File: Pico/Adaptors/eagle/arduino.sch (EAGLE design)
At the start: 6 parts, among them J1 JST-2P-SMD-PW-3410050P1

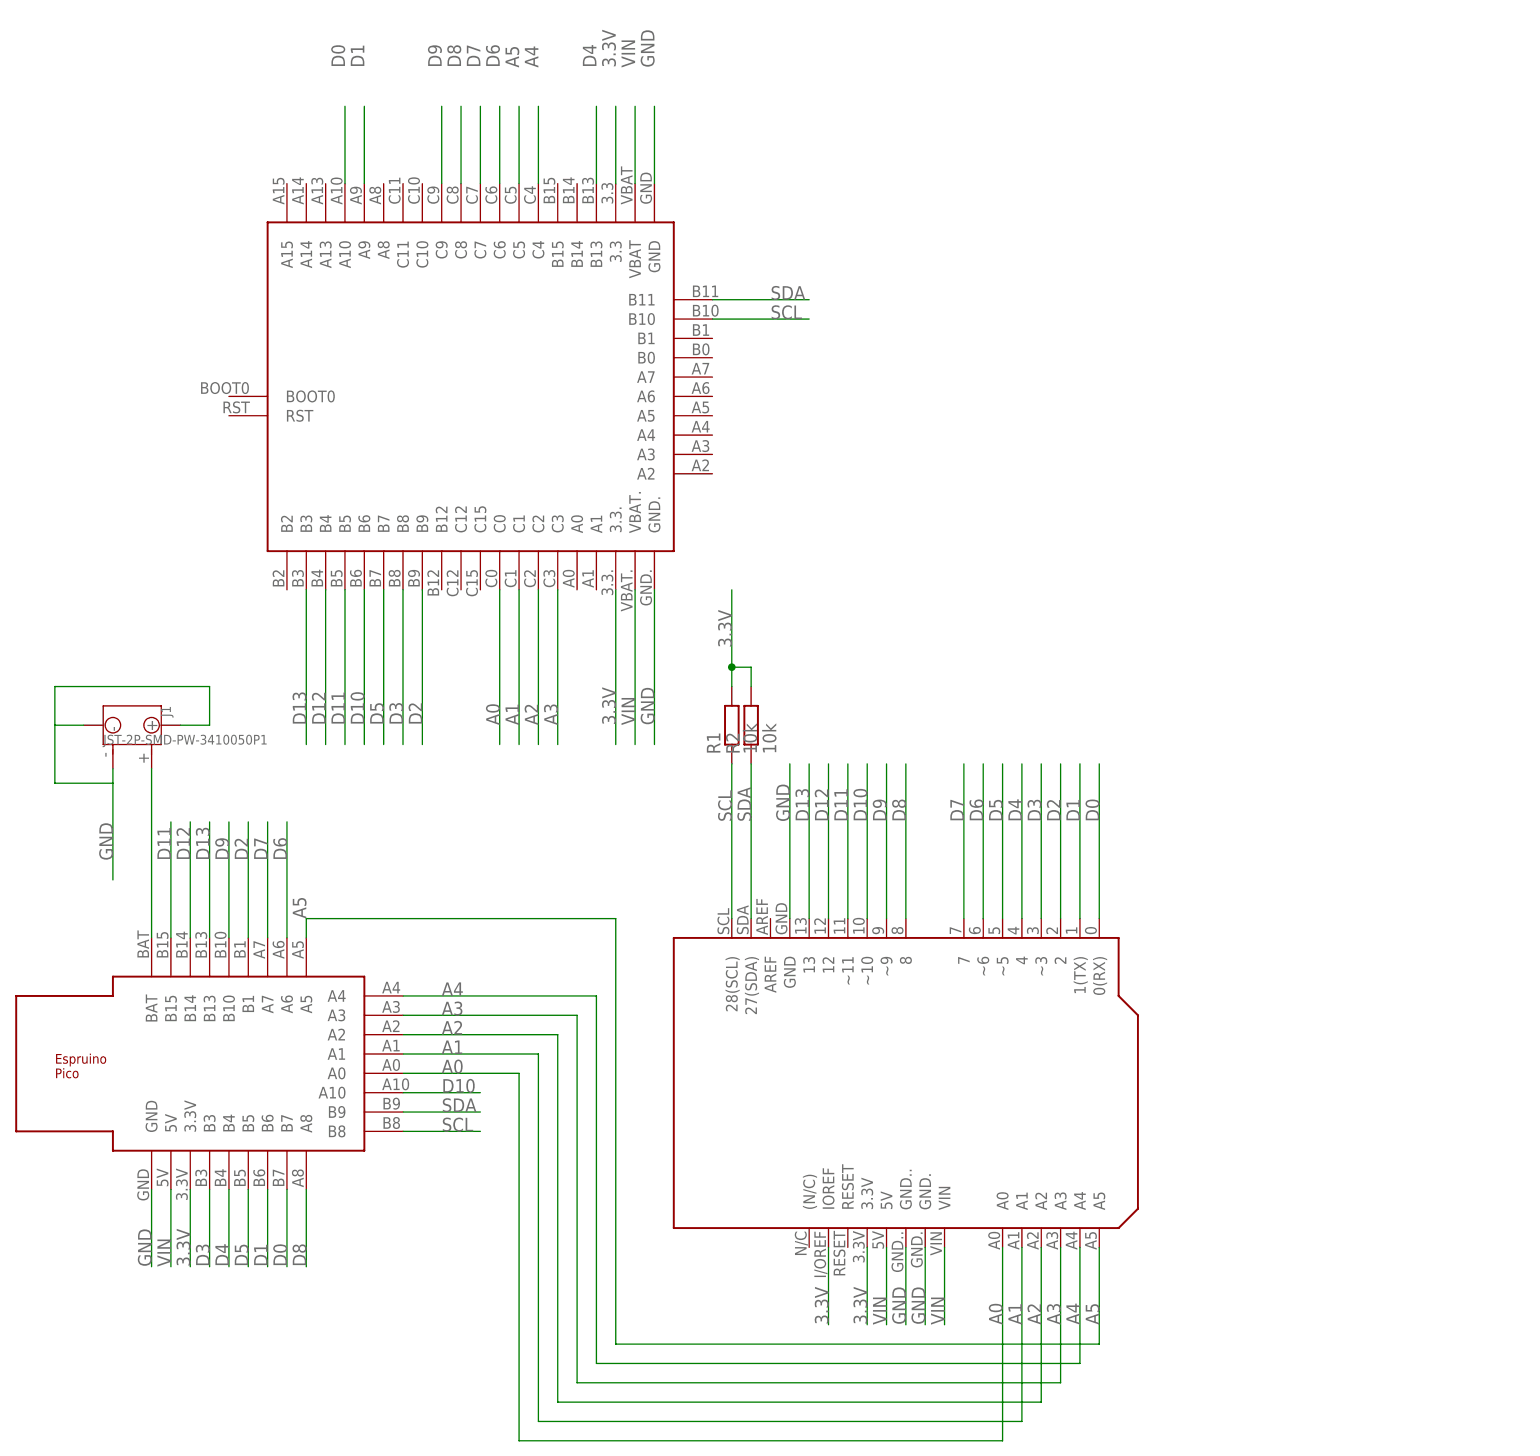
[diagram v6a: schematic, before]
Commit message: added battery charger IC
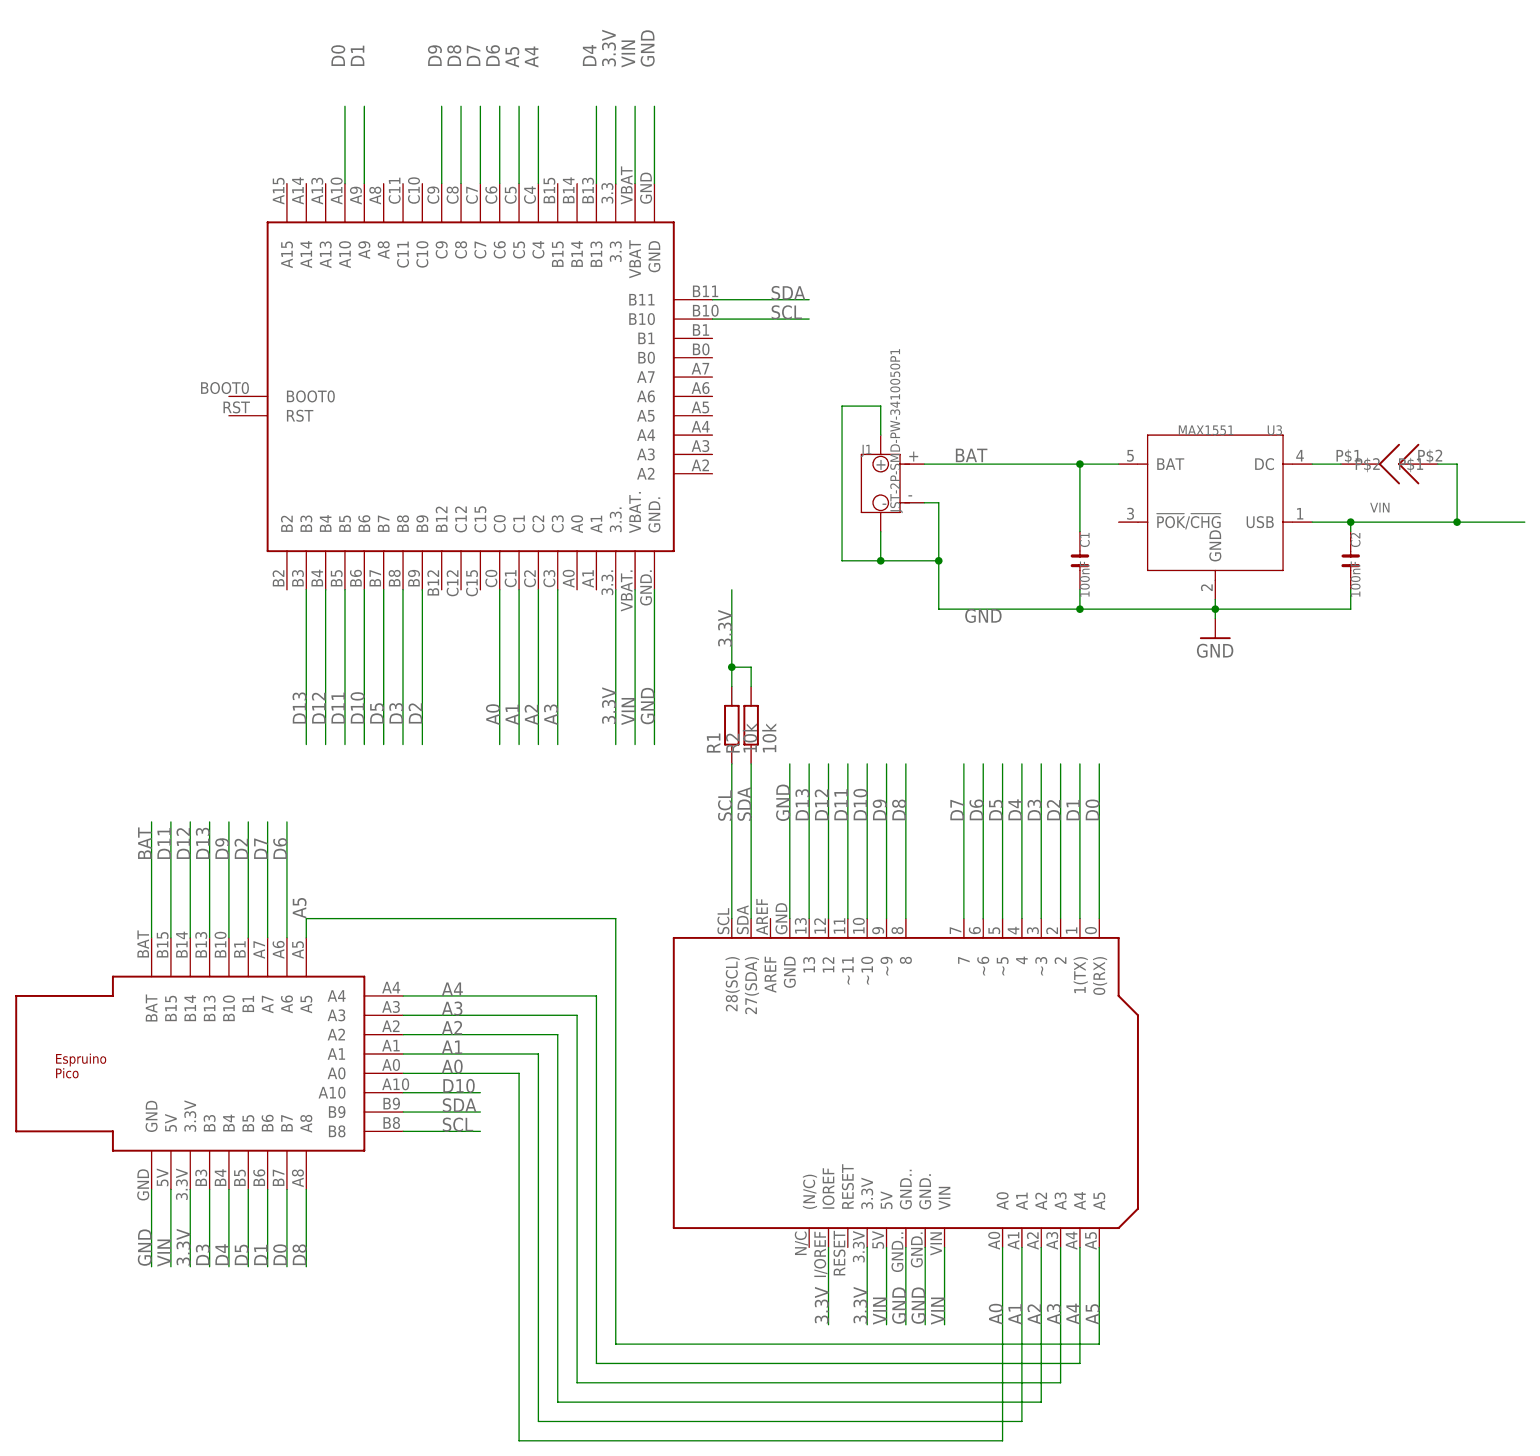
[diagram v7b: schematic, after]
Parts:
- added C1, C2: 100nF, OPL5:C-0603
- added U$4: SOLDERJUMPER, solder_jumper:SOLDERJUMPER
- added U3: MAX1551, template:MAX1551
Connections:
- removed net N$1: J1.+, U$1.BAT
- new net BAT: C1.1, J1.+, U$1.BAT, U3.BAT
- new net N$2: U$4.P$1, U3.DC
- net GND: now also C1.2, C2.2, U3.GND
- net VIN: now also C2.1, U$4.P$2, U3.USB
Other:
- moved on the sheet: J1
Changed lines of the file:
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@@
 <layer number="111" name="111" color="7" fill="1" visible="no" active="no"/>
 <layer number="112" name="tSilk" color="7" fill="1" visible="no" active="no"/>
+<layer number="113" name="IDFDebug" color="7" fill="1" visible="yes" active="yes"/>
 <layer number="116" name="Patch_BOT" color="9" fill="4" visible="yes" active="yes"/>
 <layer number="118" name="Rect_Pads" color="7" fill="1" visible="no" active="no"/>
@@
 <layer number="223" name="223bmp" color="24" fill="1" visible="no" active="no"/>
 <layer number="224" name="224bmp" color="25" fill="1" visible="no" active="no"/>
+<layer number="225" name="225bmp" color="7" fill="1" visible="yes" active="yes"/>
+<layer number="226" name="226bmp" color="7" fill="1" visible="yes" active="yes"/>
+<layer number="227" name="227bmp" color="7" fill="1" visible="yes" active="yes"/>
+<layer number="228" name="228bmp" color="7" fill="1" visible="yes" active="yes"/>
+<layer number="230" name="230bmp" color="7" fill="1" visible="no" active="yes"/>
 <layer number="248" name="Housing" color="7" fill="1" visible="no" active="no"/>
 <layer number="249" name="Edge" color="7" fill="1" visible="no" active="no"/>
@@
 <part name="R2" library="rcl" deviceset="R-EU_" device="R0805" value="10k"/>
 <part name="J1" library="OPL Eagle Library" deviceset="JST-2P-SMD-PW" device="-3410050P1"/>
+<part name="U3" library="template" deviceset="MAX1551" device="" value="MAX1551"/>
+<part name="GND26" library="supply1" deviceset="GND" device=""/>
+<part name="C2" library="OPL5" deviceset="C*" device="-0603" value="100nF"/>
+<part name="C1" library="OPL5" deviceset="C*" device="-0603" value="100nF"/>
+<part name="U$4" library="solder_jumper" deviceset="SOLDERJUMPER" device=""/>
 </parts>
 <sheets>
@@
 <instance part="R1" gate="G$1" x="60.96" y="78.74" rot="R90"/>
 <instance part="R2" gate="G$1" x="63.5" y="78.74" rot="R90"/>
-<instance part="J1" gate="J" x="-17.78" y="78.74" rot="R270"/>
+<instance part="J1" gate="J" x="80.518" y="110.49"/>
+<instance part="U3" gate="G$1" x="124.46" y="107.95" rot="MR0"/>
+<instance part="GND26" gate="1" x="124.46" y="90.17"/>
+<instance part="C2" gate="C" x="142.24" y="100.33" rot="R270"/>
+<instance part="C1" gate="C" x="106.68" y="100.33" rot="R270"/>
+<instance part="U$4" gate="G$1" x="148.59" y="113.03"/>
 </instances>
 <busses>
@@
 </segment>
 <segment>
+<pinref part="U3" gate="G$1" pin="GND"/>
+<pinref part="GND26" gate="1" pin="GND"/>
+<wire x1="124.46" y1="92.71" x2="124.46" y2="93.98" width="0.1524" layer="91"/>
+<pinref part="C1" gate="C" pin="2"/>
+<wire x1="124.46" y1="93.98" x2="124.46" y2="95.25" width="0.1524" layer="91"/>
+<wire x1="106.68" y1="96.52" x2="106.68" y2="93.98" width="0.1524" layer="91"/>
+<wire x1="106.68" y1="93.98" x2="124.46" y2="93.98" width="0.1524" layer="91"/>
+<junction x="124.46" y="93.98"/>
+<pinref part="C2" gate="C" pin="2"/>
+<wire x1="124.46" y1="93.98" x2="142.24" y2="93.98" width="0.1524" layer="91"/>
+<wire x1="142.24" y1="93.98" x2="142.24" y2="96.52" width="0.1524" layer="91"/>
 <pinref part="J1" gate="J" pin="-"/>
-<wire x1="-20.32" y1="73.025" x2="-20.32" y2="71.12" width="0.1524" layer="91"/>
-<wire x1="-20.32" y1="71.12" x2="-20.32" y2="58.42" width="0.1524" layer="91"/>
-<wire x1="-20.32" y1="71.12" x2="-27.94" y2="71.12" width="0.1524" layer="91"/>
-<wire x1="-27.94" y1="71.12" x2="-27.94" y2="78.74" width="0.1524" layer="91"/>
-<wire x1="-27.94" y1="78.74" x2="-27.94" y2="83.82" width="0.1524" layer="91"/>
-<wire x1="-27.94" y1="83.82" x2="-7.62" y2="83.82" width="0.1524" layer="91"/>
-<wire x1="-7.62" y1="83.82" x2="-7.62" y2="78.74" width="0.1524" layer="91"/>
-<wire x1="-7.62" y1="78.74" x2="-11.43" y2="78.74" width="0.1524" layer="91"/>
-<wire x1="-27.94" y1="78.74" x2="-24.13" y2="78.74" width="0.1524" layer="91"/>
+<wire x1="86.233" y1="107.95" x2="88.138" y2="107.95" width="0.1524" layer="91"/>
+<wire x1="88.138" y1="100.33" x2="88.138" y2="93.98" width="0.1524" layer="91"/>
+<wire x1="88.138" y1="107.95" x2="88.138" y2="100.33" width="0.1524" layer="91"/>
+<wire x1="88.138" y1="100.33" x2="80.518" y2="100.33" width="0.1524" layer="91"/>
+<wire x1="80.518" y1="100.33" x2="75.438" y2="100.33" width="0.1524" layer="91"/>
+<wire x1="75.438" y1="100.33" x2="75.438" y2="120.65" width="0.1524" layer="91"/>
+<wire x1="75.438" y1="120.65" x2="80.518" y2="120.65" width="0.1524" layer="91"/>
+<wire x1="80.518" y1="120.65" x2="80.518" y2="116.84" width="0.1524" layer="91"/>
+<wire x1="80.518" y1="100.33" x2="80.518" y2="104.14" width="0.1524" layer="91"/>
 <pinref part="J1" gate="J" pin="3"/>
 <pinref part="J1" gate="J" pin="4"/>
-<label x="-20.32" y="60.96" size="1.778" layer="95" rot="R90"/>
+<label x="96.52" y="93.98" size="1.778" layer="95" rot="R180"/>
+<wire x1="106.68" y1="93.98" x2="88.138" y2="93.98" width="0.1524" layer="91"/>
+<junction x="80.518" y="100.33"/>
+<junction x="88.138" y="100.33"/>
+<junction x="106.68" y="93.98"/>
 </segment>
 </net>
@@
 <wire x1="81.28" y1="10.16" x2="81.28" y2="0" width="0.1524" layer="91"/>
 <label x="81.28" y="0" size="1.778" layer="95" rot="R90"/>
+</segment>
+<segment>
+<pinref part="U3" gate="G$1" pin="USB"/>
+<wire x1="137.16" y1="105.41" x2="142.24" y2="105.41" width="0.1524" layer="91"/>
+<label x="144.78" y="106.68" size="1.27" layer="95" ratio="10"/>
+<pinref part="C2" gate="C" pin="1"/>
+<wire x1="142.24" y1="104.14" x2="142.24" y2="105.41" width="0.1524" layer="91"/>
+<junction x="142.24" y="105.41"/>
+<wire x1="142.24" y1="105.41" x2="156.21" y2="105.41" width="0.1524" layer="91"/>
+<pinref part="U$4" gate="G$1" pin="P$2"/>
+<wire x1="156.21" y1="105.41" x2="165.1" y2="105.41" width="0.1524" layer="91"/>
+<wire x1="153.67" y1="113.03" x2="156.21" y2="113.03" width="0.1524" layer="91"/>
+<wire x1="156.21" y1="113.03" x2="156.21" y2="105.41" width="0.1524" layer="91"/>
+<junction x="156.21" y="105.41"/>
+<wire x1="156.21" y1="105.41" x2="156.21" y2="105.156" width="0.1524" layer="91"/>
 </segment>
 </net>
@@
 </segment>
 </net>
-<net name="N$1" class="0">
+<net name="BAT" class="0">
 <segment>
 <pinref part="U$1" gate="G$1" pin="BAT"/>
+<wire x1="-15.24" y1="50.8" x2="-15.24" y2="66.04" width="0.1524" layer="91"/>
+<label x="-15.24" y="60.96" size="1.778" layer="95" rot="R90"/>
+</segment>
+<segment>
+<pinref part="U3" gate="G$1" pin="BAT"/>
+<pinref part="C1" gate="C" pin="1"/>
+<wire x1="86.233" y1="113.03" x2="106.68" y2="113.03" width="0.1524" layer="91"/>
+<wire x1="106.68" y1="113.03" x2="111.76" y2="113.03" width="0.1524" layer="91"/>
+<wire x1="106.68" y1="104.14" x2="106.68" y2="113.03" width="0.1524" layer="91"/>
+<junction x="106.68" y="113.03"/>
 <pinref part="J1" gate="J" pin="+"/>
-<wire x1="-15.24" y1="73.025" x2="-15.24" y2="50.8" width="0.1524" layer="91"/>
-</segment>
-</net>
+<label x="90.17" y="113.284" size="1.778" layer="95"/>
+</segment>
+</net>
+<net name="N$2" class="0">
+<segment>
+<pinref part="U3" gate="G$1" pin="DC"/>
+<pinref part="U$4" gate="G$1" pin="P$1"/>
+<wire x1="140.97" y1="113.03" x2="137.16" y2="113.03" width="0.1524" layer="91"/>
+</segment>
+</net>
